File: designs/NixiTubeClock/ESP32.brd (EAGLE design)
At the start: 32 x 49.5 mm, 19 parts, among them IC6 ESP32-WROVER-B

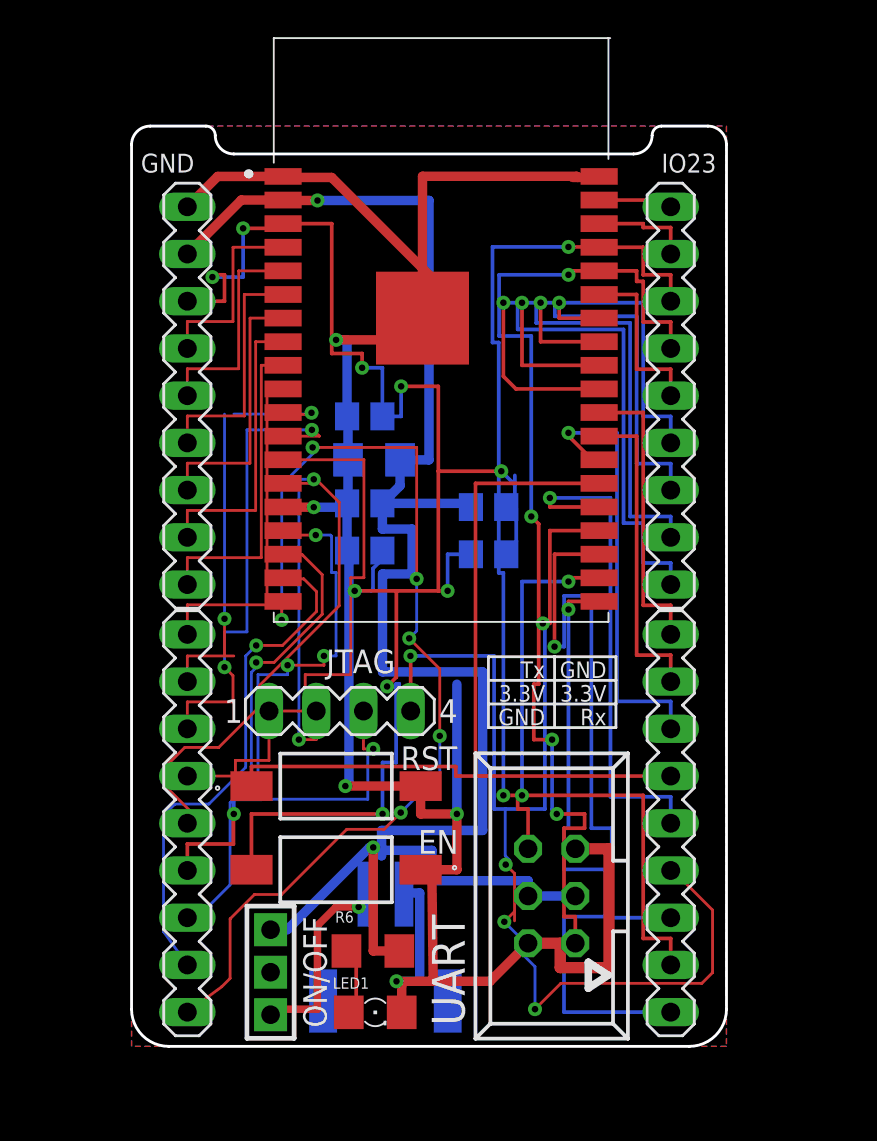
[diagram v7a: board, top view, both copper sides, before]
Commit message: final review of design and ordered from JLC PCB
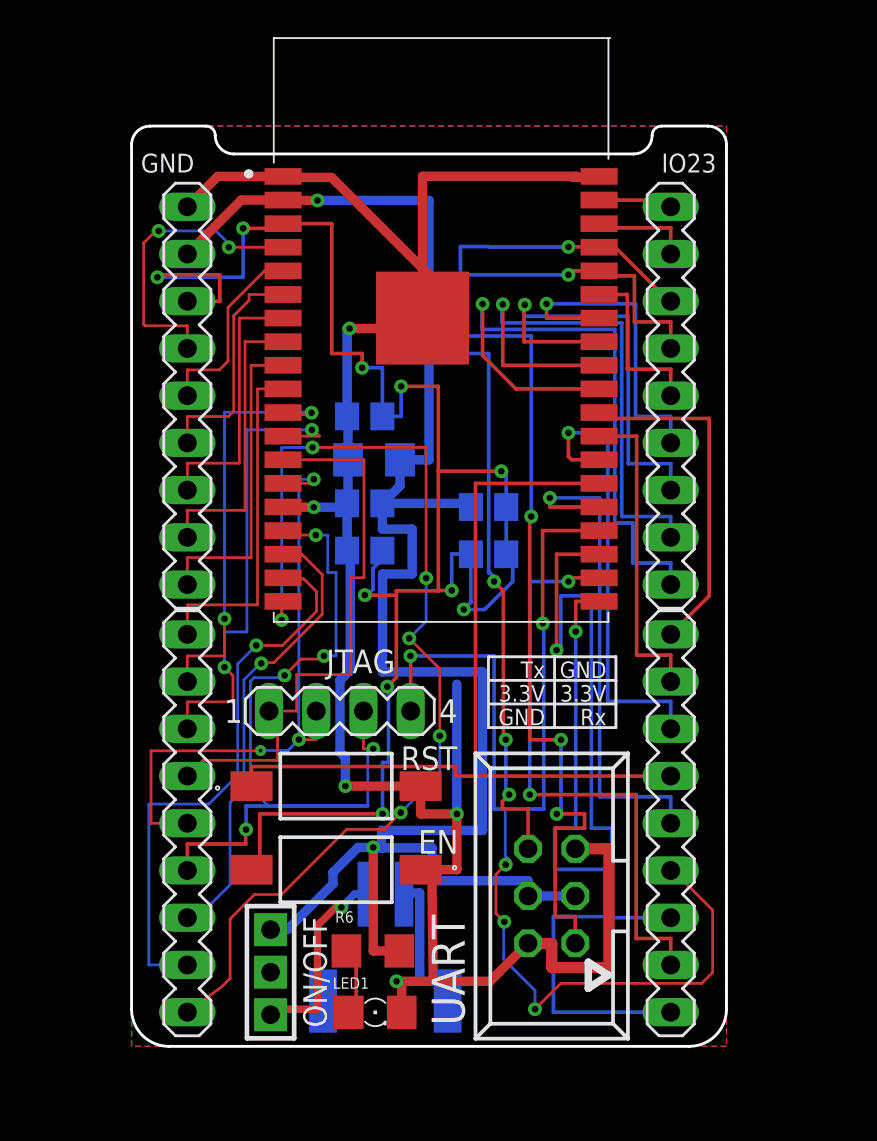
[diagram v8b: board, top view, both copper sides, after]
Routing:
- net GPIO12: track 44.0 -> 34.1 mm, vias 2 -> 3
- net EN: track 87.7 -> 97.1 mm, vias 9 -> 10
- net GPIO13: track 40.8 -> 46.8 mm
- net SEN_VP: track 10.6 -> 16.6 mm, vias 0 -> 2
- net RXD0: track 56.2 -> 60.9 mm
- net GND: track 122.8 -> 126.5 mm
- net SD3: track 27.9 -> 30.7 mm
- net NC_2: track 15.8 -> 18.5 mm
- net CLK: track 34.2 -> 36.3 mm
- net IO18: track 28.1 -> 30.1 mm
- net CMD: track 55.5 -> 57.4 mm
- net TXD0: track 46.8 -> 48.6 mm, vias 2 -> 4
- net IO19: track 22.3 -> 24.0 mm
- net IO5: track 33.6 -> 35.0 mm
- net SEN_VN: track 11.9 -> 10.4 mm
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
